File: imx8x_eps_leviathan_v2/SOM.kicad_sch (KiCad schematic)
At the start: 32 parts, among them J10 BTH-070-02-L-D-A, J9 BTH-070-02-L-D-A

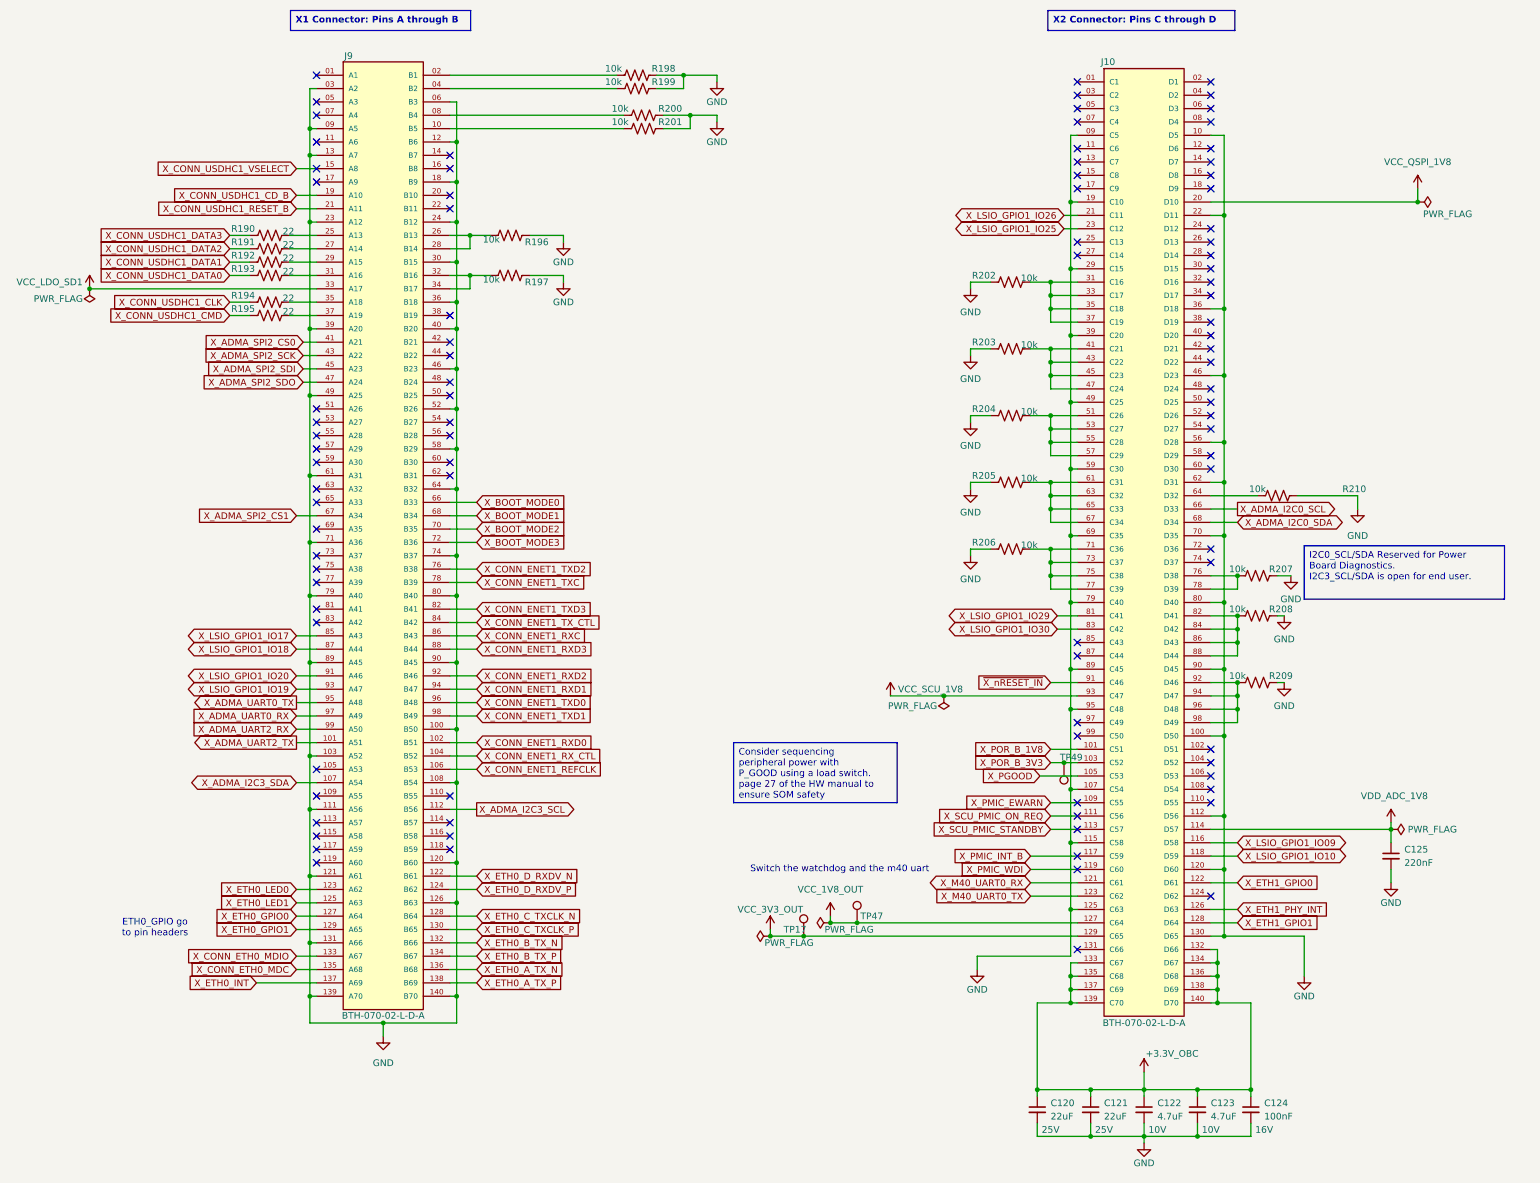
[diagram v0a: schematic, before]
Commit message: Added new PHY Jacks. Removed Not used Signals
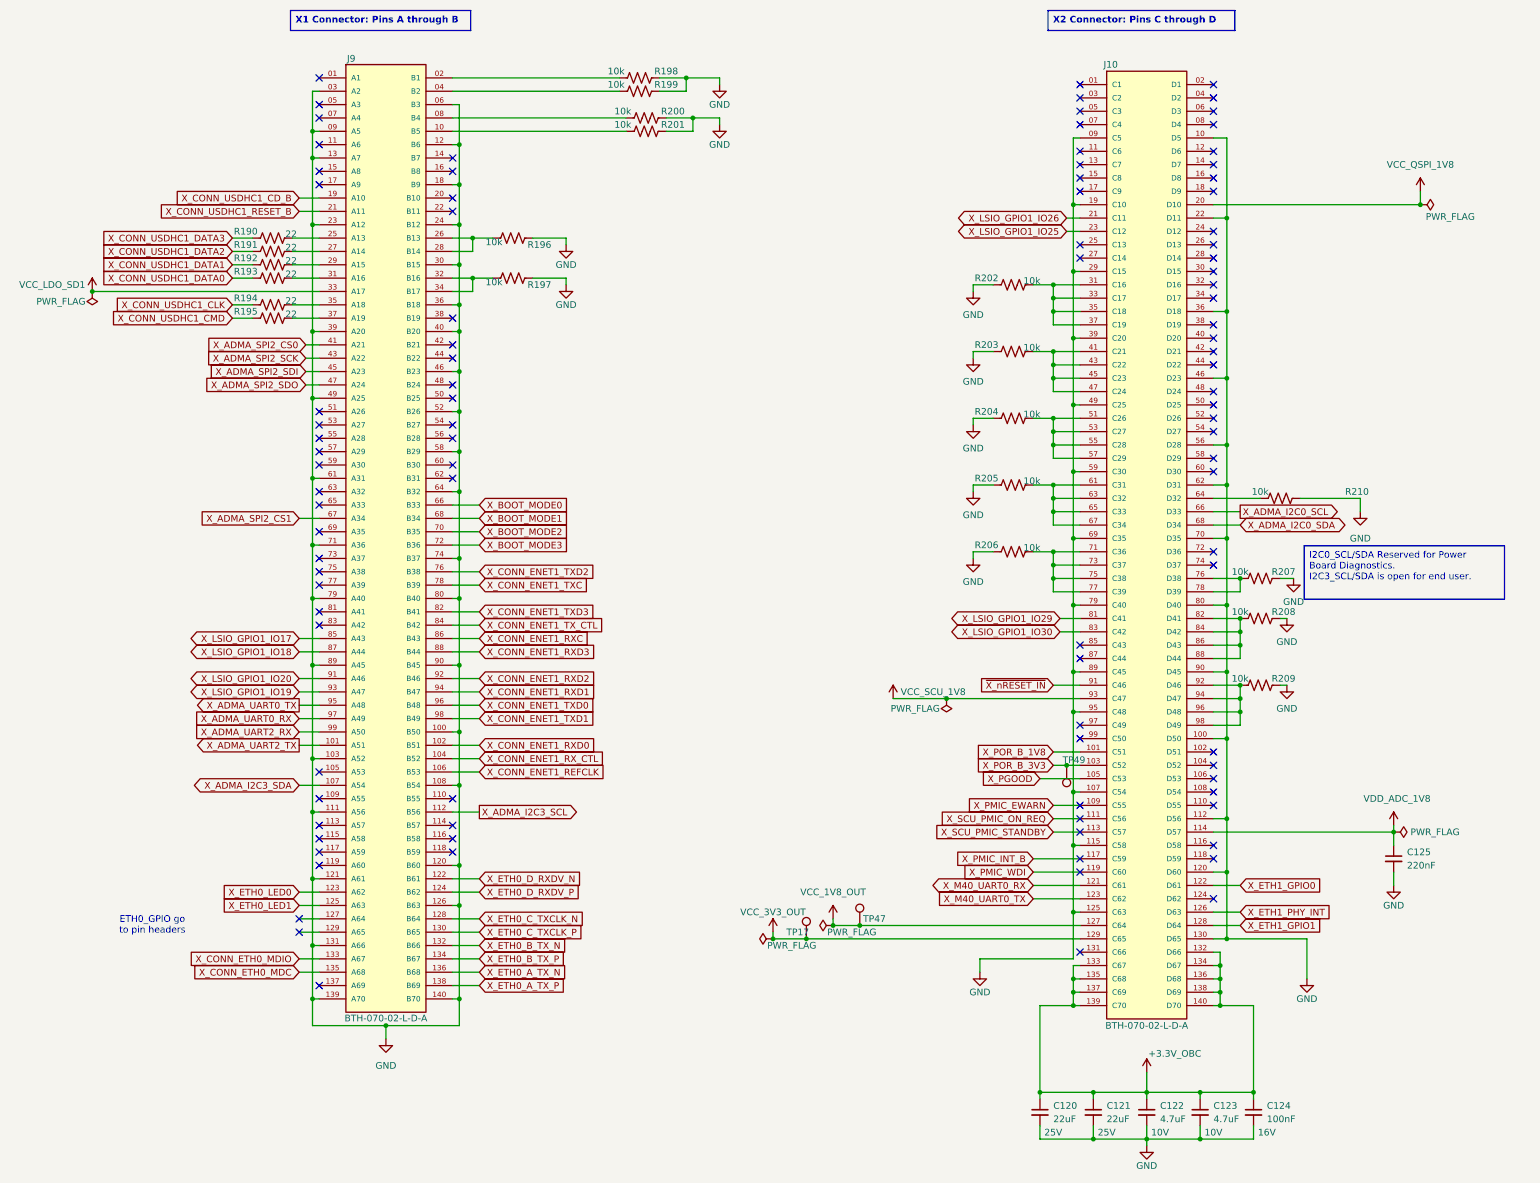
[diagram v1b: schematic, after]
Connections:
- net X_CONN_USDHC1_VSELECT: no longer names the net of J9.15 (A8)
- net X_ETH0_GPIO0: no longer names the net of J9.127 (A64)
- net X_ETH0_GPIO1: no longer names the net of J9.129 (A65)
- net X_ETH0_INT: no longer names the net of J9.137 (A69)
- net X_LSIO_GPIO1_IO09: no longer names the net of J10.116 (D58)
- net X_LSIO_GPIO1_IO10: no longer names the net of J10.118 (D59)
- no-connect marks 94 -> 99
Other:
- note removed: "Switch the watchdog and the m40 uart"
- moved on the sheet: C120, C121, C122, C123, C124, C125, J10, J9, R190, R191, R192, R193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
